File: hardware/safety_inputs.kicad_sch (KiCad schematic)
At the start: 36 parts, among them U10 TCA6416ARTWR, U11 TLP291-4, U12 TLP291-4, U9 TLP291-4

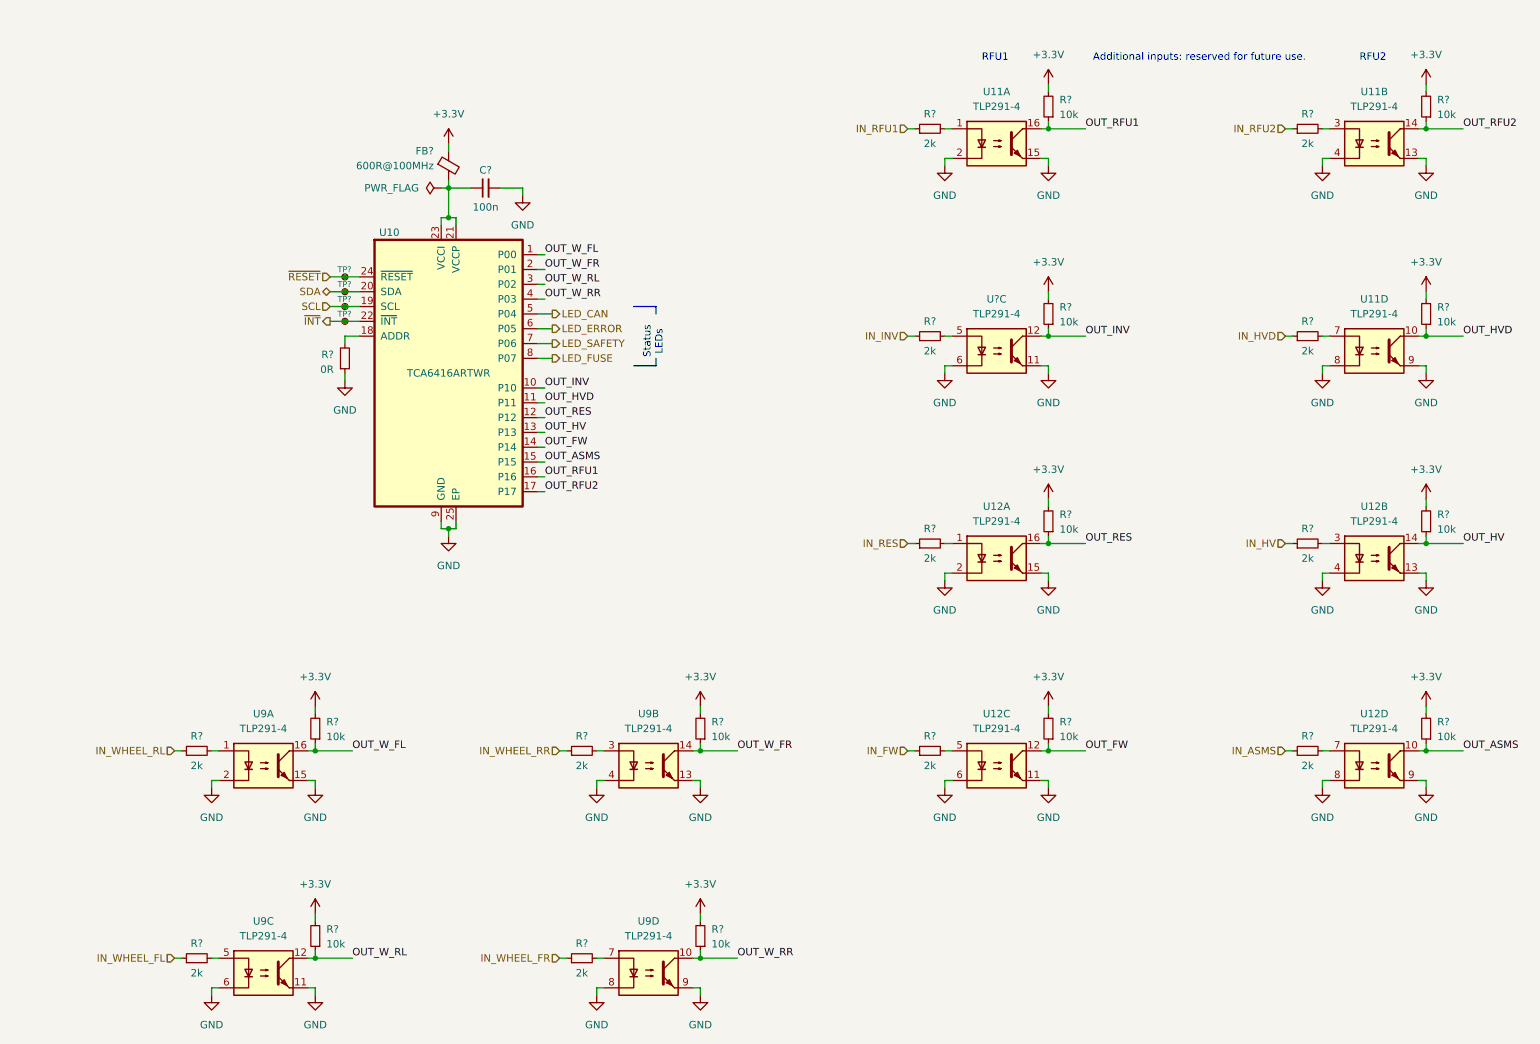
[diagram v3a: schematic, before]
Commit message: Improve the schematic according to the feedback
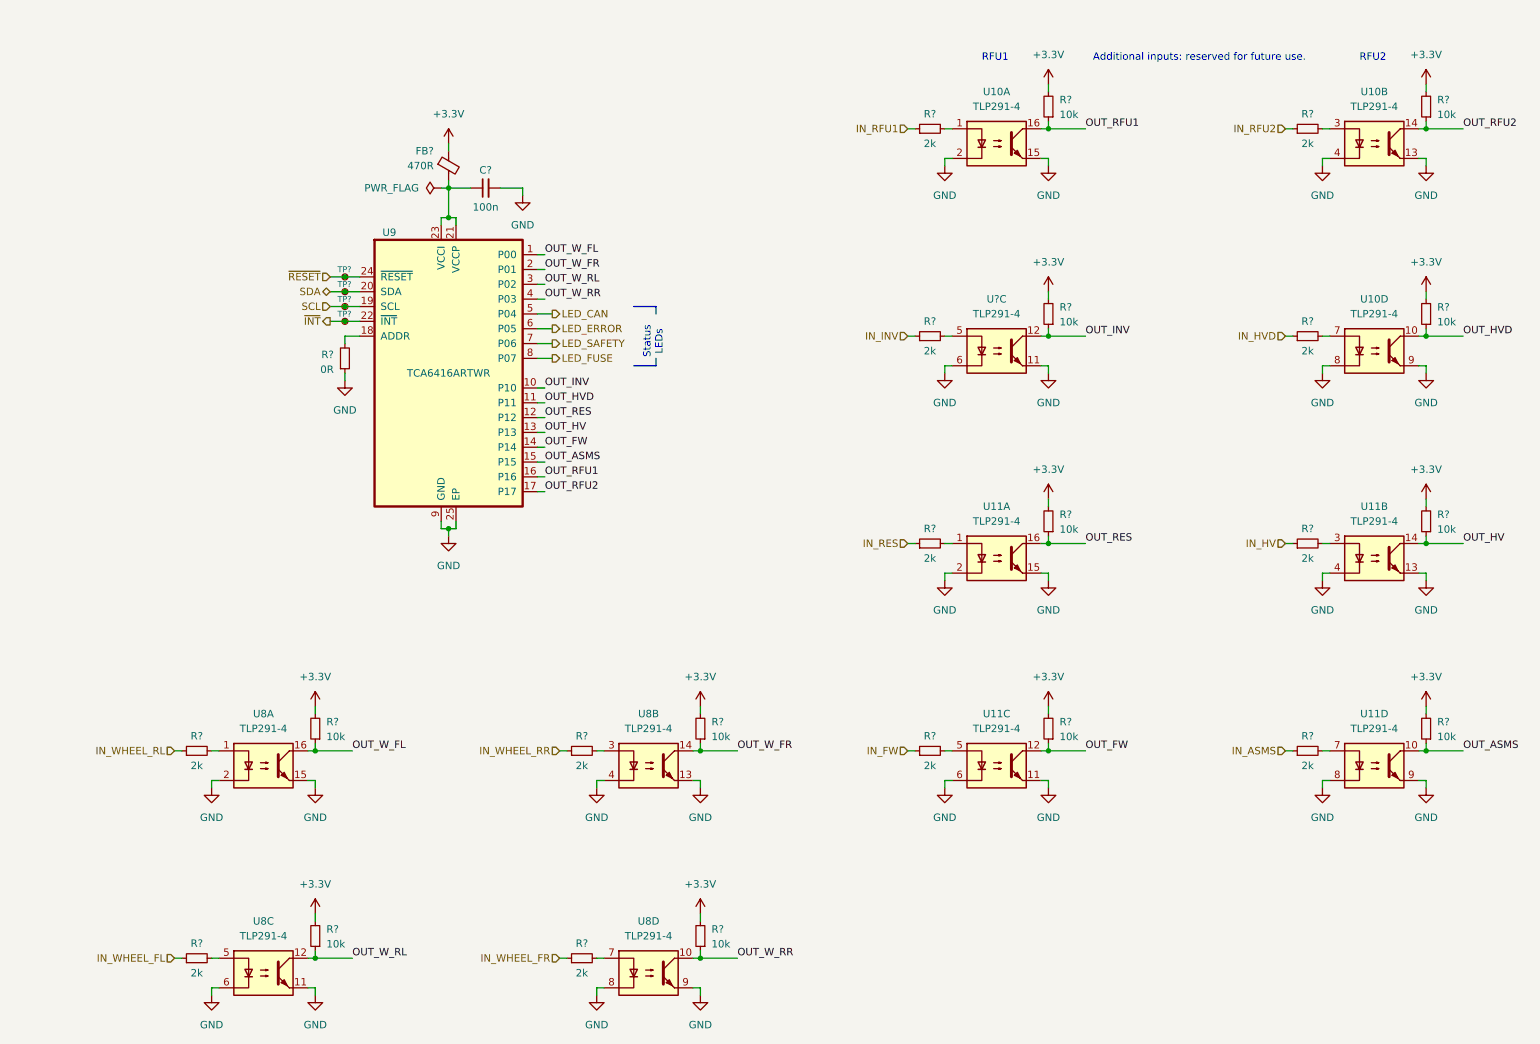
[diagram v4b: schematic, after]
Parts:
- FB?: value 600R@100MHz -> 470R
- renumbered U11 to U10, U12 to U11, U9 to U8, U10 to U9

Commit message: Add high-side drivers to the fans and pumps
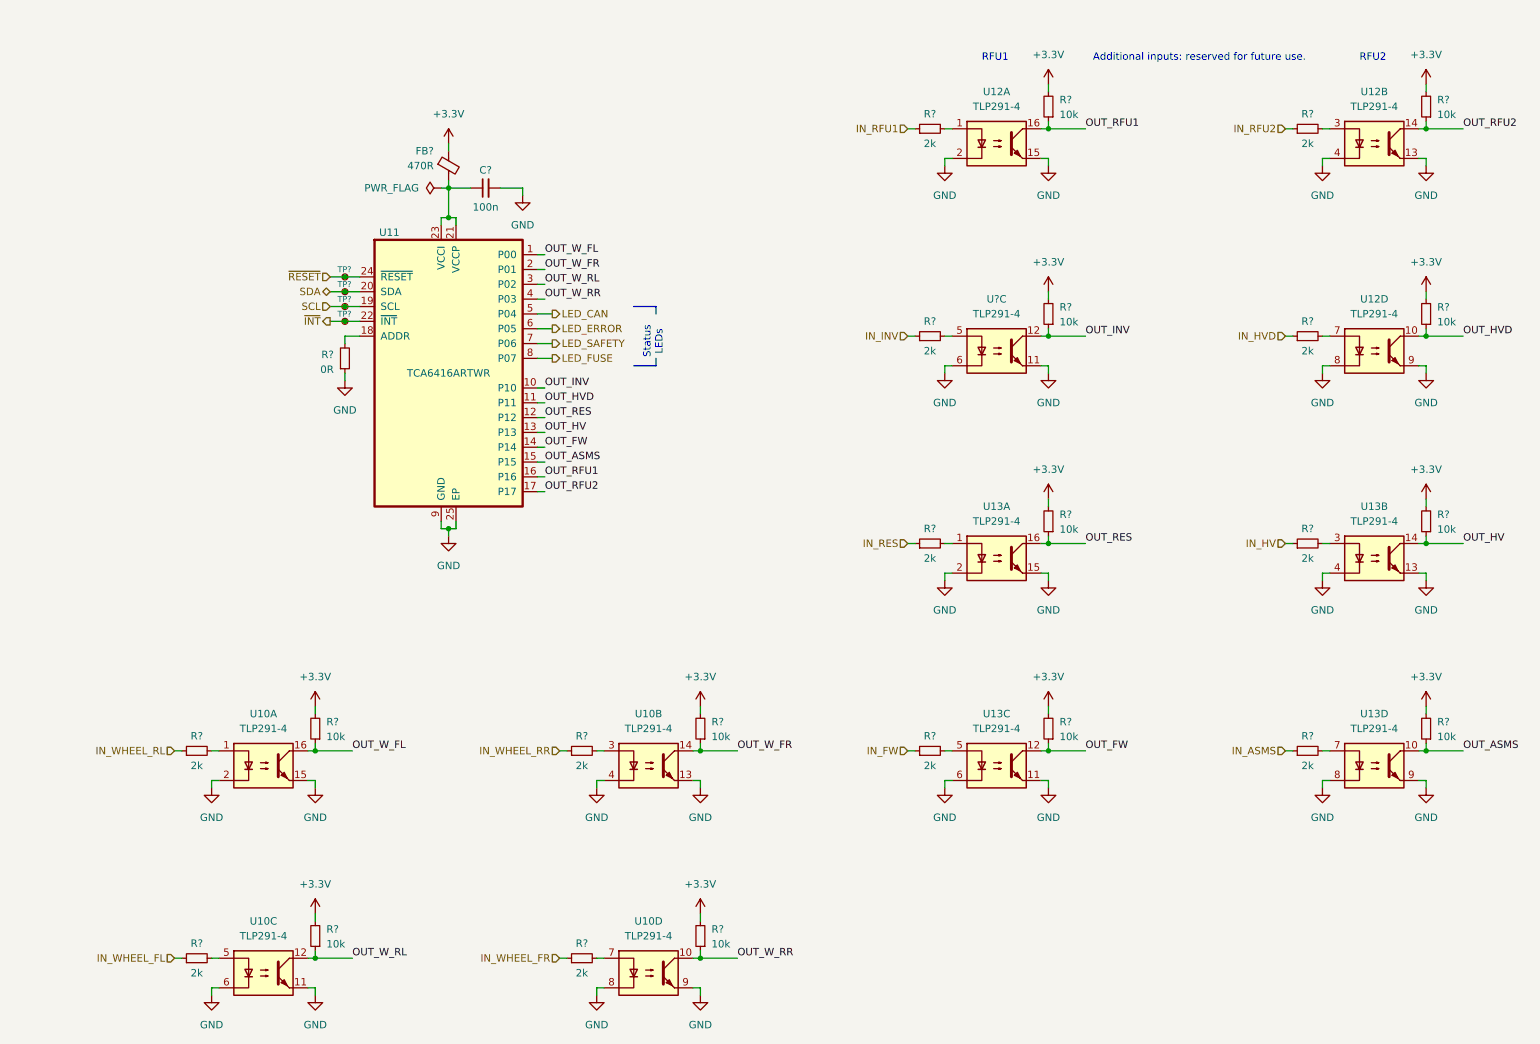
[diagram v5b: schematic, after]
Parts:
- renumbered U8 to U10, U9 to U11, U10 to U12, U11 to U13

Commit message: Improve the diagram based on the feedback
- add an input LC filter
- remove the USB connector
- add a programmer connector
- move optocouplers into a subsheet
- add a suspension tension meter IC
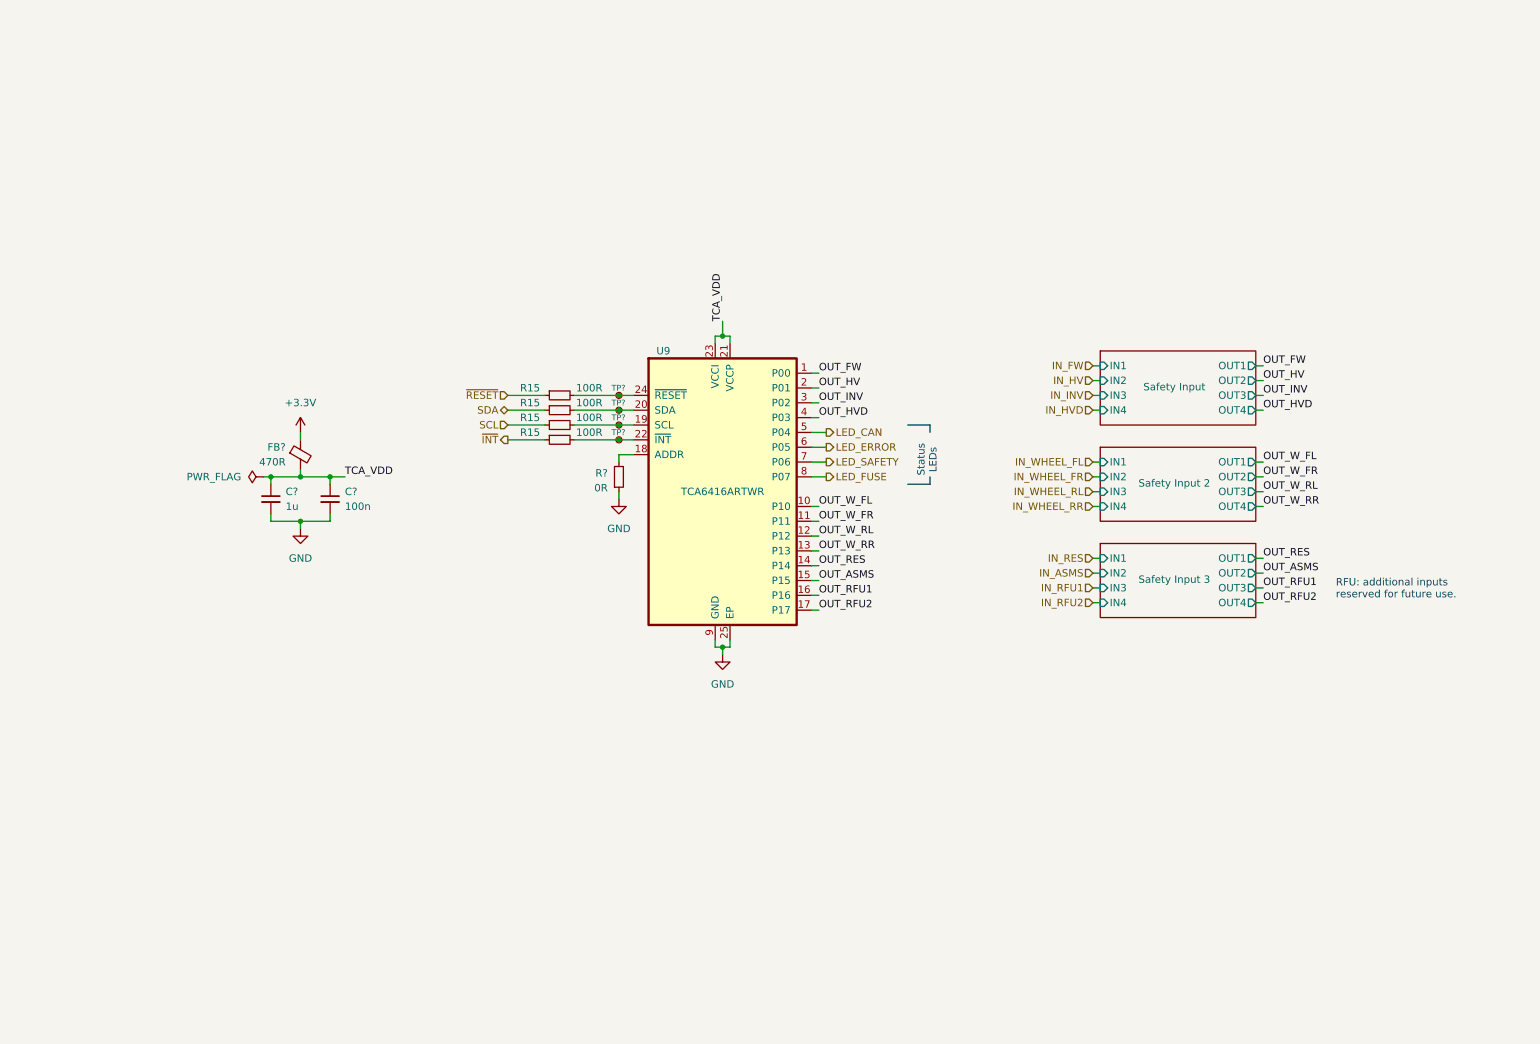
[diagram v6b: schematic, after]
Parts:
- removed C?: 100n, Capacitor_SMD:C_0603_1608Metric, symbol Device:C_Small
- removed FB?: 470R, Inductor_SMD:L_0603_1608Metric, symbol Device:FerriteBead_Small
- removed R? (x12): 2k, Resistor_SMD:R_0603_1608Metric, symbol Device:R_Small
- removed R? (x12): 10k, Resistor_SMD:R_0603_1608Metric, symbol Device:R_Small
- removed U10, U12, U13, U?: TLP291-4, Package_SO:SOIC-16_4.55x10.3mm_P1.27mm, symbol Isolator:TLP291-4
- added C?: 100n, Capacitor_SMD:C_0603_1608Metric, symbol Device:C_Small
- added C?: 1u, Capacitor_SMD:C_0603_1608Metric, symbol Device:C_Small
- added FB?: 470R, Inductor_SMD:L_0603_1608Metric, symbol Device:FerriteBead_Small
- added R15 (x4): 100R, Resistor_SMD:R_0603_1608Metric, symbol Device:R_Small
- renumbered U11 to U9
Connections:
- net +3.3V: now also FB?.1
- net GND: now also C?.2, C?.2
- net OUT_FW: now also U9.1 (P00); no longer U9.14 (P14)
- net OUT_HV: now also U9.2 (P01); no longer U9.13 (P13)
- net OUT_HVD: now also U9.4 (P03); no longer U9.11 (P11)
- net OUT_INV: now also U9.3 (P02); no longer U9.10 (P10)
- net OUT_RES: now also U9.14 (P14); no longer U9.12 (P12)
- net OUT_W_FL: now also U9.10 (P10); no longer U9.1 (P00)
- net OUT_W_FR: now also U9.11 (P11); no longer U9.2 (P01)
- net OUT_W_RL: now also U9.12 (P12); no longer U9.3 (P02)
- net OUT_W_RR: now also U9.13 (P13); no longer U9.4 (P03)
- net SCL: now also R15.1; no longer TP?.1, U9.19 (SCL)
- net SDA: now also R15.1; no longer TP?.1, U9.20 (SDA)
- net ~{INT}: now also R15.1; no longer TP?.1, U9.22 (~{INT})
- net ~{RESET}: now also R15.1; no longer TP?.1, U9.24 (~{RESET})
- net TCA_VDD: now reaches U9.21 (VCCP), U9.23 (VCCI)
- net TCA_VDD: now also C?.1, C?.1, FB?.2
- new net: R15.2, TP?.1, U9.24 (~{RESET})
- new net: R15.2, TP?.1, U9.19 (SCL)
- new net: R15.2, TP?.1, U9.20 (SDA)
- new net: R15.2, TP?.1, U9.22 (~{INT})
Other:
- added sheet Safety Input (safety_input.kicad_sch)
- added sheet Safety Input 2 (safety_input.kicad_sch)
- added sheet Safety Input 3 (safety_input.kicad_sch)
- note removed: "Additional inputs: reserved for future use."
- note removed: "RFU1"
- note removed: "RFU2"
- moved on the sheet: R?, TP?, U9
